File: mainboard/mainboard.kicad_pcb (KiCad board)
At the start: 2 copper layers, 68 x 98 mm, 62 parts, among them J1 Servo, J2 ADC Pins, J3 USB Data, J4 Button Interface, J5 Power, J6 Release Button, J7 5V GPIO, J8 GPIO Pins, Q1 2N3904, Q2 2N3904, SW1 SW_Push, U1 RP2040, U2 W25Q128JVS, U3 LSF0108PW, U4 DS1307Z+, U5 TSDP341xx, U6 TM1637, U7 LTC-4627JD, Y1 Crystal_ABM8, Y2 32.768 kHz

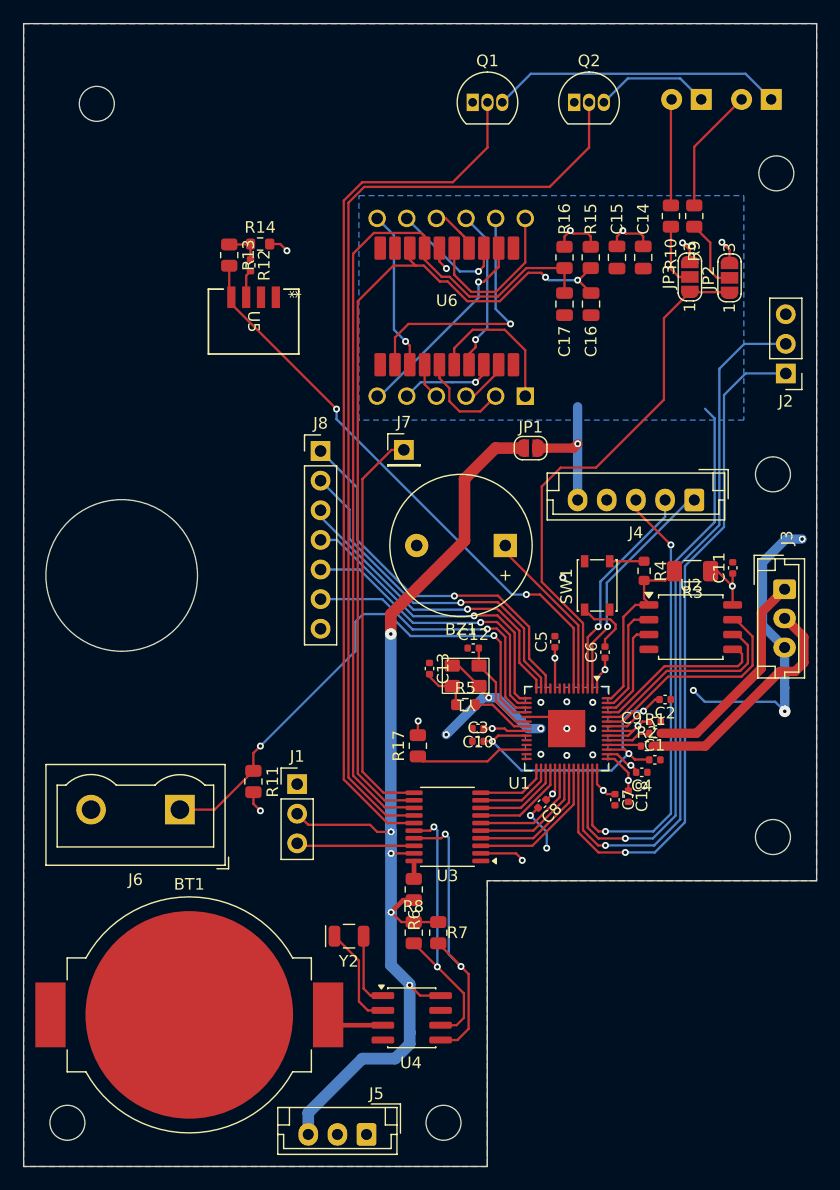
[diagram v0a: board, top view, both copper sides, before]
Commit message: updated PCB to match schematic
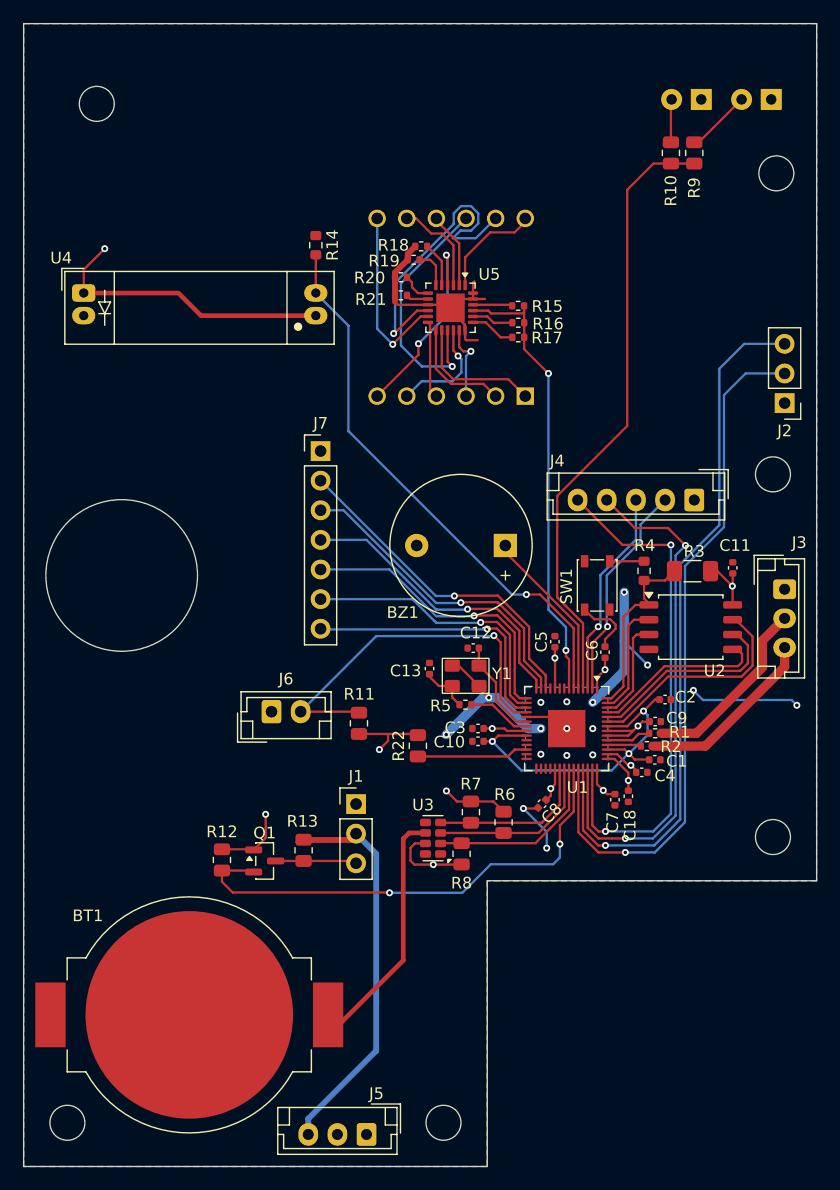
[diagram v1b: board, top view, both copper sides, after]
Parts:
- removed C14, C15: 10u, Capacitor_SMD:C_0805_2012Metric
- removed C16, C17: 100p, Capacitor_SMD:C_0805_2012Metric
- removed the J7 at (110.3, 82.5)
- removed JP1: 7-Seg, Jumper:SolderJumper-2_P1.3mm_Open_RoundedPad1.0x1.5mm
- removed JP2, JP3: PWM/POT, Jumper:SolderJumper-3_P1.3mm_Open_RoundedPad1.0x1.5mm_NumberLabels
- removed Q2: 2N3904, Package_TO_SOT_THT:TO-92_Inline
- removed the U6 at (114.0, 70.2)
- removed Y2: 32.768 kHz, Crystal:Crystal_SMD_EuroQuartz_EQ161-2Pin_3.2x1.5mm
- added R17: 10k, Resistor_SMD:R_0402_1005Metric, F.Cu at (120.2, 72.9)
- added R18: 10k, Resistor_SMD:R_0402_1005Metric, F.Cu at (111.8, 65.1)
- added R19: 10k, Resistor_SMD:R_0402_1005Metric, F.Cu at (111.2, 66.2)
- added R20: 10k, Resistor_SMD:R_0402_1005Metric, F.Cu at (110.1, 67.8)
- added R21: 10k, Resistor_SMD:R_0402_1005Metric, F.Cu at (110.1, 69.3)
- J6: footprint TerminalBlock_Wuerth:Wuerth_691311400102_P7.62mm -> Connector_JST:JST_EH_B2B-EH-A_1x02_P2.50mm_Vertical
- Q1: value 2N3904 -> BSS138; footprint Package_TO_SOT_THT:TO-92_Inline -> Package_TO_SOT_SMD:SOT-23
- R12: value 27.4 -> 10k; footprint Resistor_SMD:R_0402_1005Metric -> Resistor_SMD:R_0805_2012Metric
- R15, R16: footprint Resistor_SMD:R_0805_2012Metric -> Resistor_SMD:R_0402_1005Metric
- R5: footprint Resistor_SMD:R_0603_1608Metric -> Resistor_SMD:R_0402_1005Metric
- R6: value 20k -> 4.7k
- U3: value LSF0108PW -> RV-3028-C7; footprint Package_SO:TSSOP-20_4.4x6.5mm_P0.65mm -> Package_SON:MicroCrystal_C7_SON-8_1.5x3.2mm_P0.9mm
- U4: value DS1307Z+ -> ITR9608-F; footprint Package_SO:SOIC-8_3.9x4.9mm_P1.27mm -> OptoDevice:PIRUPT_14mm
- U5: value TSDP341xx -> TCA9535RTWR; footprint footprints:SMD4_TSSP60_VIS -> Package_DFN_QFN:WQFN-24-1EP_4x4mm_P0.5mm_EP2.45x2.45mm
- moved U4 68.2 mm to (82.9, 69.1)
- moved Q1 67.5 mm to (98.4, 117.8)
- moved R13 51.4 mm to (101.8, 116.9)
- moved R12 51.0 mm to (94.8, 117.7)
- moved U5 16.9 mm to (114.3, 70.4)
- moved J6 11.5 mm to (99.0, 105.0), turned to 0 degrees
- moved R7 10.7 mm to (116.1, 113.6)
- moved R11 10.3 mm to (106.5, 106.0)
- moved R6 9.62 mm to (118.9, 114.5)
- moved R8 7.91 mm to (115.3, 117.2), turned to 90 degrees
- moved R15 7.48 mm to (120.2, 70.2), turned to 180 degrees
- moved R16 6.86 mm to (120.2, 71.7), turned to 180 degrees
- moved R10 5.41 mm to (133.2, 57.1)
- moved R9 5.41 mm to (135.2, 57.1)
- moved J1 5.33 mm to (106.2, 112.9)
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- renumbered J8 to J7, R17 to R22, U7 to U6
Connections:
- D1 pad 1: Net-(D1-K) -> GND
- D2 pad 1: Net-(D2-K) -> GND
- J1 pad 3: /SERVO_PWM_5 -> Net-(J1-Pin_3)
- J2 pad 1: /GPIO26_ADC0 -> GND
- J2 pad 2: /GPIO27_ADC1 -> /GPIO26_ADC0
- J2 pad 3: GND -> /GPIO27_ADC1
- J3 pad 1: /USB D+ -> GND
- J3 pad 2: /USB D- -> /USB D+
- J3 pad 3: GND -> /USB D-
- J4 pad 1: /AIN1 -> GND
- J4 pad 2: /AIN2 -> /AIN1
- J4 pad 3: /BTNS -> /AIN2
- J4 pad 4: GND -> /BTNS
- J4 pad 5: /POT_OUT -> /POT
- J5 pad 1: +3.3V -> GND
- J5 pad 2: GND -> +3.3V
- J6 pad 1: /B_RELEASE -> GND
- J6 pad 2: GND -> /B_RELEASE
- J7 pad 1: /GPIO9 -> GND
- J7 pad 2: /GPIO10 -> /GPIO9
- J7 pad 3: /GPIO11 -> /GPIO10
- J7 pad 4: /GPIO12 -> /GPIO11
- J7 pad 5: /GPIO13 -> /GPIO12
- J7 pad 6: /GPIO14 -> /GPIO13
- J7 pad 7: GND -> /GPIO14
- Q1 pad 1: GND -> +3.3V
- Q1 pad 2: /D1_Q_5 -> /SERVO_PWM
- Q1 pad 3: Net-(D1-K) -> Net-(J1-Pin_3)
- R10 pad 1: Net-(JP3-C) -> /LED_PWM
- R12 pad 1: Net-(R12-Pad1) -> +3.3V
- R12 pad 2: Net-(U5-VS) -> /SERVO_PWM
- R13 pad 1: Net-(R12-Pad1) -> +5V
- R13 pad 2: /IR_REC -> Net-(J1-Pin_3)
- R14 pad 1: Net-(R12-Pad1) -> GND
- R14 pad 2: +3.3V -> /IR
- R15 pad 1: /POT_OUT -> /7-SEG_PWM
- R15 pad 2: /7SEG_CLK_5 -> Net-(U5-~{INT})
- R16 pad 1: /POT_OUT -> /7-SEG_PWM
- R16 pad 2: /7SEG_DIO_5 -> /7-SEG_SDA
- R6 pad 1: Net-(U3-EN) -> +3.3V
- R6 pad 2: +5V -> /RTC_SCL
- R7 pad 1: +5V -> +3.3V
- R7 pad 2: /RTC_SDA_5 -> /RTC_SDA
- R8 pad 1: +5V -> +3.3V
- R8 pad 2: /RTC_SCL_5 -> /RTC_INT
- R9 pad 1: Net-(JP2-C) -> /LED_PWM
- U1 pad 29: /GPIO_3V -> unconnected-(U1-GPIO18-Pad29)
- U1 pad 30: /7SEG_CLK_3 -> unconnected-(U1-GPIO19-Pad30)
- U1 pad 31: /7SEG_DIO_3 -> unconnected-(U1-GPIO20-Pad31)
- U1 pad 32: /D2_Q_3 -> unconnected-(U1-GPIO21-Pad32)
- U1 pad 34: /D1_Q_3 -> /RTC_SDA
- U1 pad 35: /RTC_SCL_3 -> /RTC_SCL
- U1 pad 36: /RTC_SDA_3 -> /RTC_INT
- U1 pad 37: /SERVO_PWM_3 -> /SERVO_PWM
- U1 pad 40: /POT_OUT -> /BTNS
- U1 pad 41: /BTNS -> /POT
- U1 pad 6: /IR_REC -> /IR
- U1 pad 7: unconnected-(U1-GPIO5-Pad7) -> /7-SEG_PWM
- U3 pad 1: GND -> unconnected-(U3-CLKOUT-Pad1)
- U3 pad 2: +3.3V -> /RTC_INT
- U3 pad 3: /SERVO_PWM_3 -> /RTC_SCL
- U3 pad 4: /RTC_SDA_3 -> /RTC_SDA
- U3 pad 5: /RTC_SCL_3 -> GND
- U3 pad 6: /D1_Q_3 -> Net-(BT1-+)
- U3 pad 7: /D2_Q_3 -> +3.3V
- U3 pad 8: /7SEG_DIO_3 -> unconnected-(U3-EVI-Pad8)
- U4 pad 1: Net-(U4-X1) -> +3.3V
- U4 pad 2: Net-(U4-X2) -> GND
- U4 pad 3: Net-(BT1-+) -> +3.3V
- U4 pad 4: GND -> /IR
- U5 pad 1: GND -> Net-(U5-P00)
- U5 pad 2: unconnected-(U5-NC-Pad2) -> Net-(U5-P01)
- U5 pad 3: Net-(U5-VS) -> Net-(U5-P02)
- U5 pad 4: /IR_REC -> Net-(U5-P03)
- U6 pad 1: Net-(U6-SEG5/KS5) -> Net-(U5-P14)
- U6 pad 10: Net-(U6-SEG6/KS6) -> Net-(U5-P15)
- U6 pad 11: Net-(U6-SEG1/KS1) -> Net-(U5-P10)
- U6 pad 12: Net-(U6-GRID1) -> Net-(U5-P00)
- U6 pad 2: Net-(U6-SEG4/KS4) -> Net-(U5-P13)
- U6 pad 3: Net-(U6-SEG8/KS8) -> Net-(U5-P17)
- U6 pad 4: Net-(U6-SEG3/KS3) -> Net-(U5-P12)
- U6 pad 5: Net-(U6-SEG7/KS7) -> Net-(U5-P16)
- U6 pad 6: Net-(U6-GRID4) -> Net-(U5-P03)
- U6 pad 7: Net-(U6-SEG2/KS2) -> Net-(U5-P11)
- U6 pad 8: Net-(U6-GRID3) -> Net-(U5-P02)
- U6 pad 9: Net-(U6-GRID2) -> Net-(U5-P01)
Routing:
- net /D2_Q_5: track 82.7 -> 0.00 mm
- net /POT_OUT: track 77.2 -> 0.00 mm, vias 7 -> 0
- net /7SEG_DIO_5: track 75.9 -> 0.00 mm
- net /D1_Q_5: track 75.3 -> 0.00 mm
- net /7SEG_CLK_5: track 74.0 -> 0.00 mm, vias 2 -> 0
- net +5V: track 91.4 -> 33.7 mm, vias 5 -> 0
- net /IR_REC: track 50.3 -> 0.00 mm, vias 2 -> 0
- net /IR: track 0.00 -> 47.8 mm, vias 0 -> 1
- net /POT: track 0.00 -> 45.1 mm, vias 0 -> 2
- net /SERVO_PWM: track 0.00 -> 42.5 mm, vias 0 -> 2
- net +3.3V: track 43.9 -> 86.1 mm, vias 13 -> 14
- net /7-SEG_PWM: track 0.00 -> 39.3 mm, vias 0 -> 2
- net /GPIO_5V: track 34.9 -> 0.00 mm
- net Net-(U5-P10): track 0.00 -> 27.2 mm, vias 0 -> 1
- net /RTC_SDA_5: track 25.9 -> 0.00 mm, vias 2 -> 0
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- removed copper zone on B.Cu, net /POT_OUT

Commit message: organizational changes; made board smaller, made mount holes more uniform
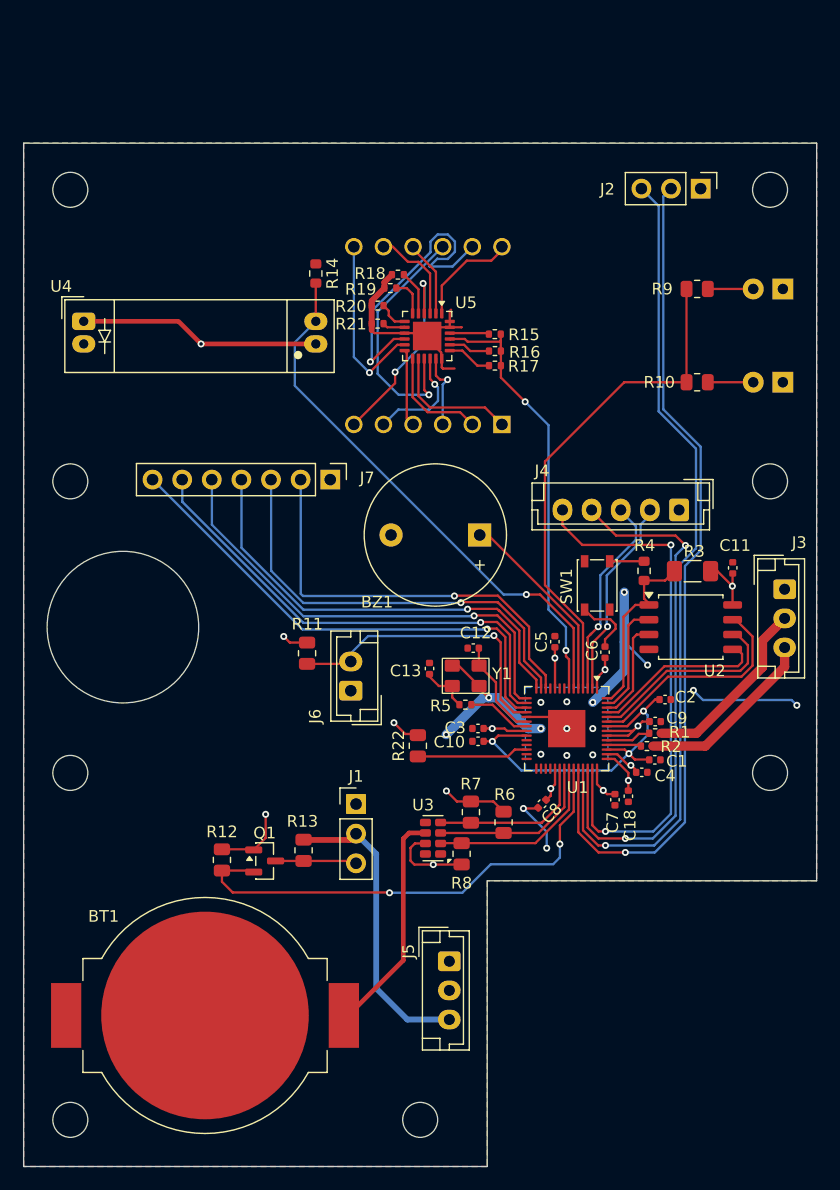
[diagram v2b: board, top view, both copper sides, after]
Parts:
- moved D2 25.2 mm to (142.8, 76.8)
- moved R10 19.8 mm to (135.5, 76.8), turned to 0 degrees
- moved J2 19.7 mm to (135.8, 60.1), turned to -90 degrees
- moved J5 16.5 mm to (114.2, 126.4), turned to -90 degrees
- moved D1 16.3 mm to (142.8, 68.8)
- moved R9 11.7 mm to (135.5, 68.8), turned to 0 degrees
- moved R11 7.48 mm to (102.0, 100.0), turned to -90 degrees
- moved J6 7.03 mm to (105.8, 103.2), turned to 90 degrees
- moved R15 3.15 mm to (118.2, 72.6)
- moved R18 3.15 mm to (109.8, 67.5)
- moved R19 3.15 mm to (109.2, 68.7)
- moved R20 3.15 mm to (108.1, 70.2)
- moved R21 3.15 mm to (108.1, 71.7)
- moved U5 3.15 mm to (112.3, 72.8)
- moved U6 3.15 mm to (118.8, 80.4)
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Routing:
- net /GPIO14: track 23.5 -> 43.2 mm
- net /GPIO13: track 24.4 -> 41.7 mm
- net /GPIO12: track 25.4 -> 40.2 mm
- net /GPIO26_ADC0: track 60.6 -> 73.0 mm
- net /GPIO11: track 25.9 -> 38.2 mm
- net /GPIO27_ADC1: track 61.7 -> 71.7 mm
- net /GPIO10: track 28.0 -> 37.4 mm
- net /LED_PWM: track 52.8 -> 44.1 mm
- net +5V: track 33.7 -> 26.1 mm
- net /GPIO9: track 29.0 -> 36.4 mm
- net /B_RELEASE: track 32.7 -> 25.5 mm
- net +3.3V: track 86.1 -> 79.6 mm, vias 14 -> 15
- net Net-(BT1-+): track 21.6 -> 19.6 mm
- net /Buzzer: track 15.1 -> 17.1 mm
- net /POT: track 45.1 -> 46.8 mm
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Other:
- board size 68 x 98 mm -> 68 x 87.8 mm

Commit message: added test points
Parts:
- added TP1: GND, TestPoint:TestPoint_Pad_4.0x4.0mm, F.Cu at (97.5, 109.0)
- added TP2: 5V, TestPoint:TestPoint_Pad_D2.0mm, F.Cu at (105.5, 140.0)
- added TP3: 3V3, TestPoint:TestPoint_Pad_D2.0mm, F.Cu at (80.5, 121.2)
- added TP4: 1V1, TestPoint:TestPoint_Pad_D1.5mm, F.Cu at (134.7, 116.8)
- added TP5: Pot, TestPoint:TestPoint_Pad_D1.5mm, F.Cu at (126.2, 79.7)
- U6: footprint Display_7Segment:CA56-12EWA -> Display_7Segment:CA56-12SURKWA
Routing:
- net +5V: track 26.1 -> 38.9 mm
- net +1V1: track 31.4 -> 42.0 mm, vias 3 -> 4
- net /POT: track 46.8 -> 55.7 mm
- net +3.3V: track 79.6 -> 82.7 mm, vias 15 -> 16
- net /LED_PWM: track 44.1 -> 46.8 mm
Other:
- outline, holes or cut-outs redrawn

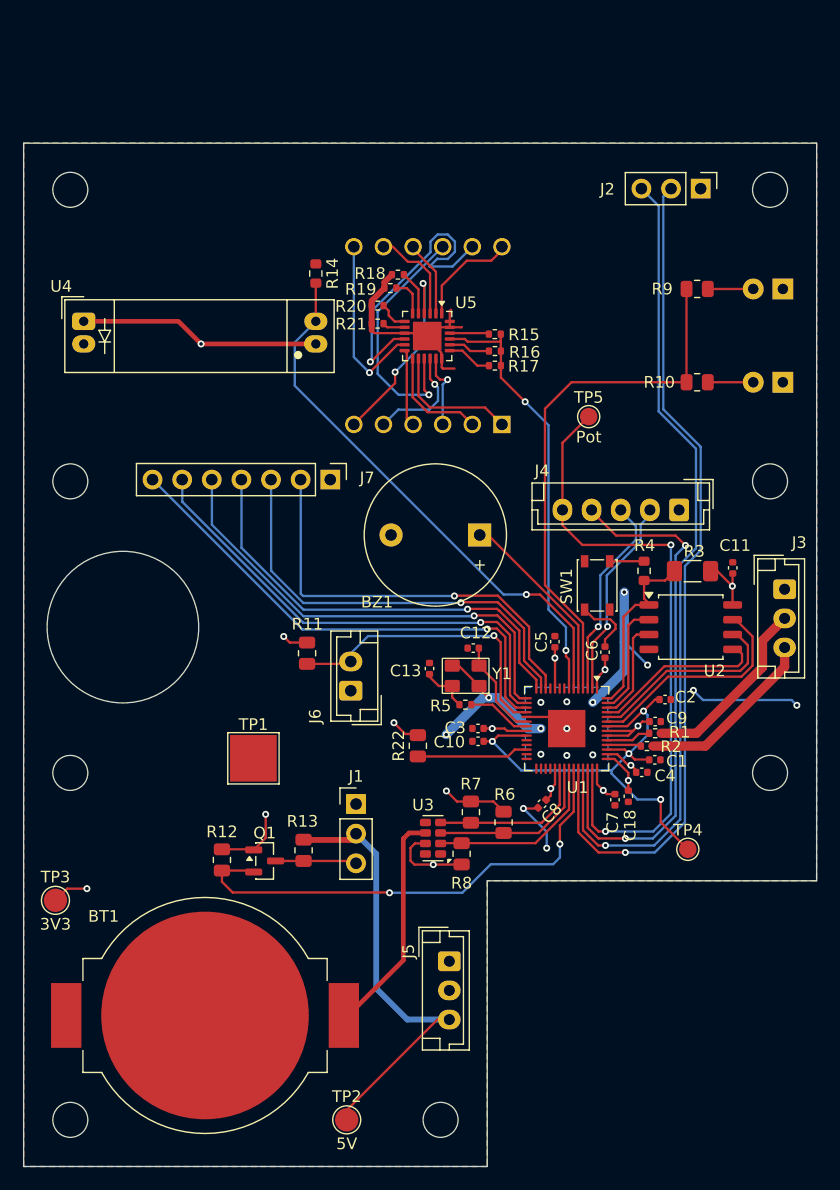
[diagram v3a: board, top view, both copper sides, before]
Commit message: Replaced 3v plane with gnd plane. Rerouted all 3v connections Redid 7seg/io expander traces (improved organization) Made LEDs individually controllable
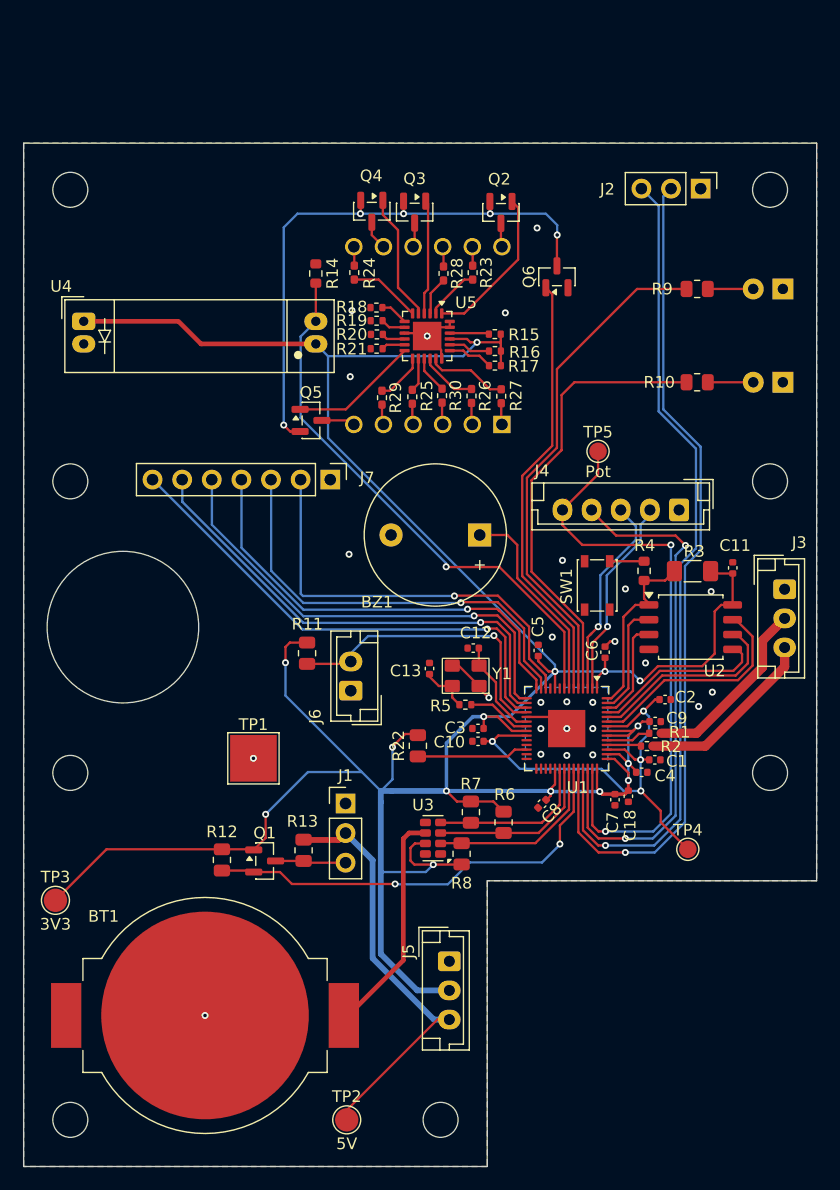
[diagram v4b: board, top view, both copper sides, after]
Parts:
- added Q2: 2N7002, Package_TO_SOT_SMD:SOT-23, F.Cu at (118.7, 62.2)
- added Q3: 2N7002, Package_TO_SOT_SMD:SOT-23, F.Cu at (111.3, 62.2)
- added Q4: 2N7002, Package_TO_SOT_SMD:SOT-23, F.Cu at (107.6, 62.1)
- added Q5: 2N7002, Package_TO_SOT_SMD:SOT-23, F.Cu at (102.4, 80.0)
- added Q6: 2N7002, Package_TO_SOT_SMD:SOT-23, F.Cu at (123.5, 67.7)
- added R23: 200, Resistor_SMD:R_0402_1005Metric_Pad0.72x0.64mm_HandSolder, F.Cu at (116.2, 67.4)
- added R24: 200, Resistor_SMD:R_0402_1005Metric_Pad0.72x0.64mm_HandSolder, F.Cu at (106.1, 67.3)
- added R25: 200, Resistor_SMD:R_0402_1005Metric_Pad0.72x0.64mm_HandSolder, F.Cu at (111.1, 78.0)
- added R26: 200, Resistor_SMD:R_0402_1005Metric_Pad0.72x0.64mm_HandSolder, F.Cu at (116.2, 77.9)
- added R27: 200, Resistor_SMD:R_0402_1005Metric_Pad0.72x0.64mm_HandSolder, F.Cu at (118.7, 78.0)
- added R28: 200, Resistor_SMD:R_0402_1005Metric_Pad0.72x0.64mm_HandSolder, F.Cu at (113.8, 67.4)
- added R29: 200, Resistor_SMD:R_0402_1005Metric_Pad0.72x0.64mm_HandSolder, F.Cu at (108.5, 78.1)
- added R30: 200, Resistor_SMD:R_0402_1005Metric_Pad0.72x0.64mm_HandSolder, F.Cu at (113.6, 77.9)
- moved R18 3.37 mm to (108.0, 70.3)
- moved TP5 3.08 mm to (127.0, 82.7)
- moved R19 3.03 mm to (108.0, 71.5)
- moved R20 2.47 mm to (108.0, 72.7)
- moved R21 2.15 mm to (108.0, 73.9)
- moved C5 1.61 mm to (121.9, 99.8)
- moved J1 0.90 mm to (105.3, 112.9)
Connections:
- R10 pad 1: /LED_PWM -> /RED_LED
- R15 pad 1: /7-SEG_PWM -> +3.3V
- R16 pad 1: /7-SEG_PWM -> +3.3V
- R17 pad 1: /7-SEG_PWM -> +3.3V
- R18 pad 1: Net-(U5-P04) -> Net-(U5-P06)
- R19 pad 1: Net-(U5-P05) -> Net-(U5-P07)
- R20 pad 1: Net-(U5-P06) -> Net-(U5-P10)
- R21 pad 1: Net-(U5-P07) -> Net-(U5-P11)
- R9 pad 1: /LED_PWM -> /WHITE_LED
- U1 pad 4: /LED_PWM -> /RED_LED
- U1 pad 5: /Buzzer -> /WHITE_LED
- U1 pad 6: /IR -> /7-SEG_PWM
- U1 pad 7: /7-SEG_PWM -> /Buzzer
- U1 pad 8: unconnected-(U1-GPIO6-Pad8) -> /IR
- U5 pad 1: Net-(U5-P00) -> /7-Segment/CC1
- U5 pad 12: Net-(U5-P12) -> /7-Segment/CC4
- U5 pad 13: Net-(U5-P13) -> /7-Segment/LED_g
- U5 pad 14: Net-(U5-P14) -> /7-Segment/LED_c
- U5 pad 15: Net-(U5-P15) -> /7-Segment/DP
- U5 pad 16: Net-(U5-P16) -> /7-Segment/LED_d
- U5 pad 17: Net-(U5-P17) -> /7-Segment/LED_e
- U5 pad 2: Net-(U5-P01) -> /7-Segment/LED_a
- U5 pad 21: /7-SEG_PWM -> +3.3V
- U5 pad 3: Net-(U5-P02) -> /7-Segment/LED_f
- U5 pad 4: Net-(U5-P03) -> /7-Segment/CC2
- U5 pad 5: Net-(U5-P04) -> /7-Segment/CC3
- U5 pad 6: Net-(U5-P05) -> /7-Segment/LED_b
- U6 pad 1: Net-(U5-P14) -> Net-(U6-e)
- U6 pad 10: Net-(U5-P15) -> Net-(U6-f)
- U6 pad 11: Net-(U5-P10) -> Net-(U6-a)
- U6 pad 12: Net-(U5-P00) -> Net-(Q2-D)
- U6 pad 2: Net-(U5-P13) -> Net-(U6-d)
- U6 pad 3: Net-(U5-P17) -> Net-(U6-DPX)
- U6 pad 4: Net-(U5-P12) -> Net-(U6-c)
- U6 pad 5: Net-(U5-P16) -> Net-(U6-g)
- U6 pad 6: Net-(U5-P03) -> Net-(Q5-D)
- U6 pad 7: Net-(U5-P11) -> Net-(U6-b)
- U6 pad 8: Net-(U5-P02) -> Net-(Q4-D)
- U6 pad 9: Net-(U5-P01) -> Net-(Q3-D)
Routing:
- net +3.3V: track 82.7 -> 272.7 mm, vias 16 -> 15
- net GND: track 71.3 -> 16.9 mm, vias 17 -> 26
- net Net-(Q2-S): track 0.00 -> 49.8 mm, vias 0 -> 5
- net /LED_PWM: track 46.8 -> 0.00 mm
- net /WHITE_LED: track 0.00 -> 44.2 mm
- net /RED_LED: track 0.00 -> 39.5 mm
- net Net-(U5-P10): track 27.2 -> 2.07 mm, vias 1 -> 0
- net Net-(U5-P15): track 21.6 -> 0.00 mm, vias 1 -> 0
- net Net-(U5-P03): track 17.3 -> 0.00 mm, vias 2 -> 0
- net /7-Segment/CC1: track 0.00 -> 13.7 mm
- net Net-(U5-P11): track 15.4 -> 2.03 mm, vias 1 -> 0
- net Net-(U5-P14): track 11.4 -> 0.00 mm
- net /7-Segment/CC4: track 0.00 -> 11.0 mm
- net /7-Segment/CC3: track 0.00 -> 11.0 mm
- net /7-Segment/CC2: track 0.00 -> 9.84 mm
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- removed copper zone on B.Cu, net +3.3V
